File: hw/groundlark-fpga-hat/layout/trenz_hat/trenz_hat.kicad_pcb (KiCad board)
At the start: 2 copper layers, 120 parts

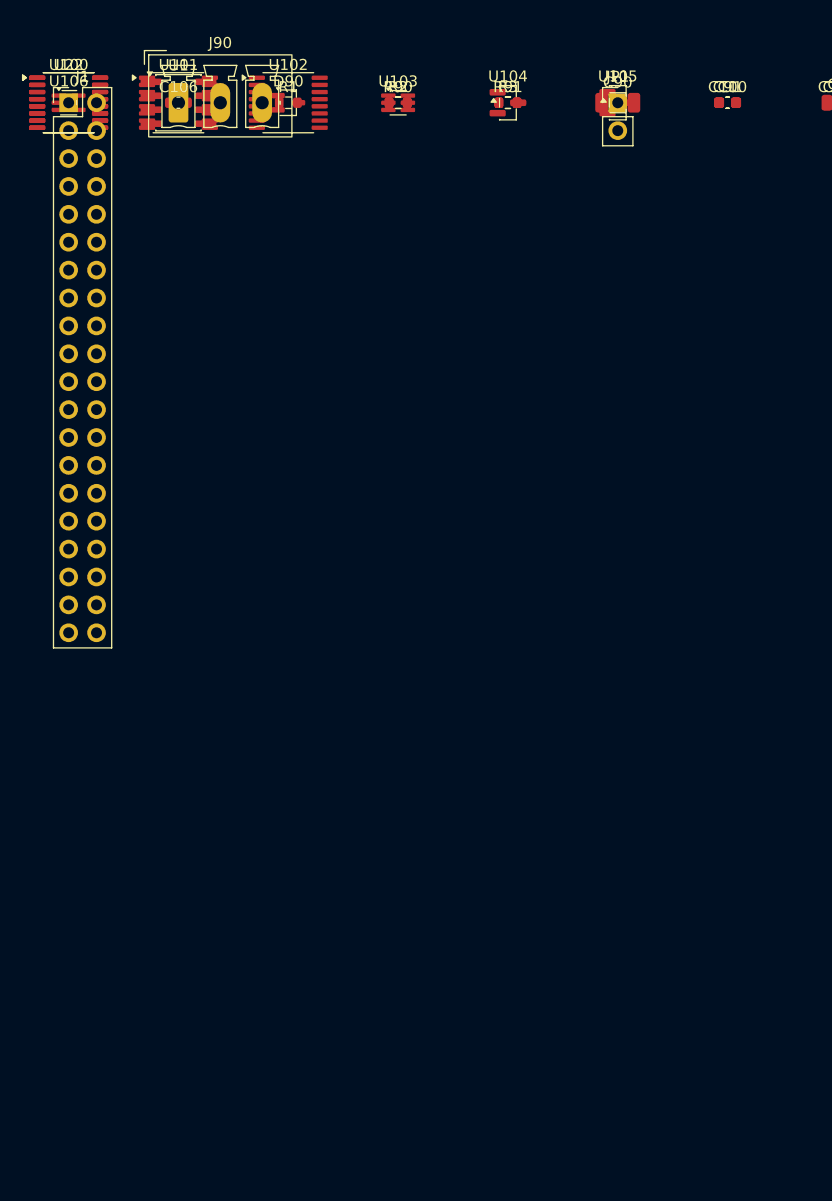
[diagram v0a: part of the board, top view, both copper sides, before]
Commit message: Use horizontal geophone connector and publish detailed enclosure render
Synchronize J90 routing, native SES, assembly mapping, enclosure fit, models and validation. Add a 4K clear-PETG README render and derive assembly PDF part identities from package procurement. Preserve Git-normalized source bindings and original validation/render input hashes. Generated JLCPCB packages remain local.
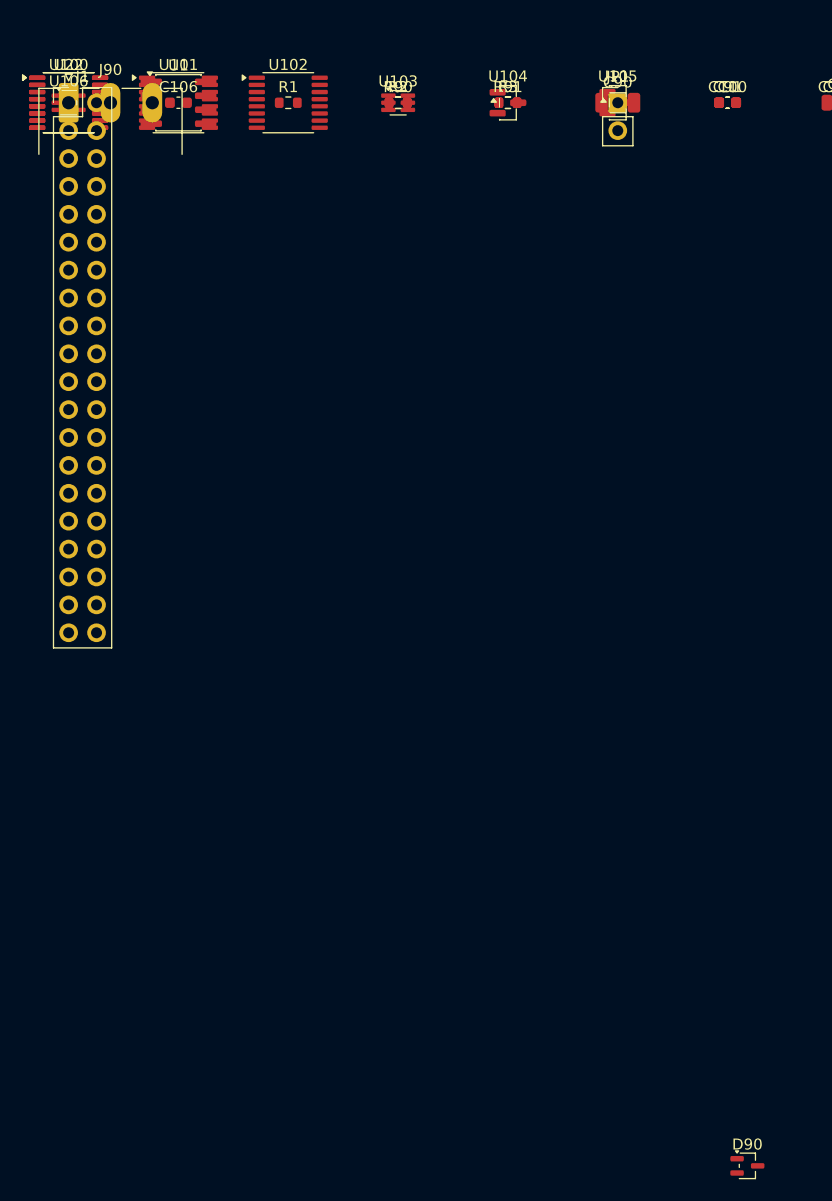
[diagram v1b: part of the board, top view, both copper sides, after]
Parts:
- J90: footprint elec:Connector_Phoenix_MC__PhoenixContact_MCV_1,5_3-G-3.81_1x03_P3.81mm_Vertical -> elec:Connector_Phoenix_MC__PhoenixContact_MC_1,5_3-G-3.81_1x03_P3.81mm_Horizontal
- moved D90 105.4 mm to (61.8, 96.8)
- moved J90 10.0 mm to (0.00, 0.00)

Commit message: Add TI Pi power supervision and expand DAQHAT enclosure
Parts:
- added C110: , elec:PWR_C_1210_3225Metric, F.Cu at (1350.0, 0.00)
- added C111: , elec:PWR_C_1210_3225Metric, F.Cu at (1360.0, 0.00)
- added C112: , elec:PWR_C_1210_3225Metric, F.Cu at (1370.0, 0.00)
- added C130: , elec:SUP_C_0805_2012Metric, F.Cu at (50.0, 0.00)
- added C131: , elec:PWR_C_1206_3216Metric, F.Cu at (60.0, 0.00)
- added C132: , elec:PWR_C_1206_3216Metric, F.Cu at (80.0, 0.00)
- added C133: , elec:PWR_C_1206_3216Metric, F.Cu at (90.0, 0.00)
- added C134: , elec:PWR_C_0603_1608Metric, F.Cu at (100.0, 0.00)
- added C135: , elec:PWR_CP_Elec_6.3x7.7, F.Cu at (110.0, 0.00)
- added C136: , elec:PWR_C_1210_3225Metric, F.Cu at (120.0, 0.00)
- added C137: , elec:PWR_C_1210_3225Metric, F.Cu at (130.0, 0.00)
- added C138: , elec:PWR_C_1210_3225Metric, F.Cu at (140.0, 0.00)
- added C139: , elec:SUP_C_0603_1608Metric, F.Cu at (190.0, 0.00)
- added C140: , elec:SUP_C_0805_2012Metric, F.Cu at (200.0, 0.00)
- added C141: , elec:PWR_C_0603_1608Metric, F.Cu at (230.0, 0.00)
- added C142: , elec:SUP_C_0805_2012Metric, F.Cu at (240.0, 0.00)
- added C143: , elec:SUP_C_0603_1608Metric, F.Cu at (250.0, 0.00)
- added C144: , elec:SUP_C_0603_1608Metric, F.Cu at (270.0, 0.00)
- added C145: , elec:SUP_C_0603_1608Metric, F.Cu at (300.0, 0.00)
- added C24: , elec:Capacitor_SMD__C_0603_1608Metric, F.Cu at (1190.0, 0.00)
- added C86: , elec:PWR_C_1206_3216Metric, F.Cu at (1310.0, 0.00)
- added C87: , elec:PWR_C_1206_3216Metric, F.Cu at (1320.0, 0.00)
- added C88: , elec:PWR_C_0603_1608Metric, F.Cu at (1330.0, 0.00)
- added C89: , elec:PWR_CP_Elec_6.3x7.7, F.Cu at (1340.0, 0.00)
- added D130: , elec:PWR_D_SMA, F.Cu at (20.0, 0.00)
- added D131: , elec:SUP_D_SMA, F.Cu at (30.0, 0.00)
- added D80: , elec:PWR_D_SMA, F.Cu at (1220.0, 0.00)
- added D81: , elec:PWR_D_SMA, F.Cu at (1230.0, 0.00)
- added F130: , elec:SUP_Fuse_1206_3216Metric, F.Cu at (10.0, 0.00)
- added J130: , elec:SUP_PhoenixContact_MC_1,5_2-G-3.81_1x02_P3.81mm_Horizontal, F.Cu at (0.00, 0.00)
- added J131: , elec:SUP_PinHeader_1x05_P1.27mm_Vertical, F.Cu at (370.0, 0.00)
- added JP130: , elec:SUP_PinHeader_1x02_P2.54mm_Vertical, F.Cu at (380.0, 0.00)
- added Q130: , elec:SUP_SOT-23, F.Cu at (310.0, 0.00)
- added Q131: , elec:SUP_SOT-23, F.Cu at (340.0, 0.00)
- added R120: , elec:PWR_R_0603_1608Metric, F.Cu at (1250.0, 0.00)
- added R121: , elec:PWR_R_0603_1608Metric, F.Cu at (1260.0, 0.00)
- added R122: , elec:PWR_R_0603_1608Metric, F.Cu at (1270.0, 0.00)
- added R123: , elec:PWR_R_0603_1608Metric, F.Cu at (1280.0, 0.00)
- added R124: , elec:PWR_R_0603_1608Metric, F.Cu at (1290.0, 0.00)
- added R130: , elec:PWR_R_0603_1608Metric, F.Cu at (150.0, 0.00)
- added R131: , elec:SUP_R_0603_1608Metric, F.Cu at (160.0, 0.00)
- added R132: , elec:PWR_R_0603_1608Metric, F.Cu at (170.0, 0.00)
- added R133: , elec:SUP_R_0603_1608Metric, F.Cu at (210.0, 0.00)
- added R134: , elec:SUP_R_0603_1608Metric, F.Cu at (260.0, 0.00)
- added R135: , elec:SUP_R_0603_1608Metric, F.Cu at (280.0, 0.00)
- added R136: , elec:SUP_R_0603_1608Metric, F.Cu at (290.0, 0.00)
- added R137: , elec:PWR_R_0603_1608Metric, F.Cu at (320.0, 0.00)
- added R138: , elec:PWR_R_0603_1608Metric, F.Cu at (330.0, 0.00)
- added R139: , elec:PWR_R_0603_1608Metric, F.Cu at (350.0, 0.00)
- added R140: , elec:PWR_R_0603_1608Metric, F.Cu at (360.0, 0.00)
- added R141: , elec:PWR_R_0603_1608Metric, F.Cu at (0.00, 0.00)
- added SW80: , elec:PWR_SW_SPDT_PCM12, F.Cu at (1300.0, 0.00)
- added U130: , elec:SUP_QFN-32-1EP_5x5mm_P0.5mm_EP3.45x3.45mm, F.Cu at (220.0, 0.00)
- added U131: , elec:SUP_SOT-23-5, F.Cu at (40.0, 0.00)
- added U132: , elec:PWR_Texas_B3QFN-14-1EP_5x5.5mm_P0.65mm, F.Cu at (70.0, 0.00)
- added U133: , elec:SUP_Texas_WSON10_DQC0010A, F.Cu at (180.0, 0.00)
- added U23: , elec:Groundlark__DLVR_E1BS, F.Cu at (1180.0, 0.00)
- added U80: , elec:PWR_Texas_B3QFN-14-1EP_5x5.5mm_P0.65mm, F.Cu at (1240.0, 0.00)
- F80: footprint elec:TZ_TZ_FUSE -> elec:PWR_Fuse_1206_3216Metric
- J83: footprint elec:TZ_TZ_POWER -> elec:PWR_BarrelJack_CUI_PJ-102AH_Horizontal
- moved C106 1160.0 mm to (1170.0, 0.00)
- moved U106 1160.0 mm to (1160.0, 0.00)
- moved C100 860.0 mm to (920.0, 0.00)
- moved C101 860.0 mm to (930.0, 0.00)
- moved C102 860.0 mm to (940.0, 0.00)
- moved C103 860.0 mm to (950.0, 0.00)
- moved C104 860.0 mm to (960.0, 0.00)
- moved C105 860.0 mm to (970.0, 0.00)
- moved R100 860.0 mm to (980.0, 0.00)
- moved R101 860.0 mm to (990.0, 0.00)
- moved R102 860.0 mm to (1000.0, 0.00)
- moved R103 860.0 mm to (1010.0, 0.00)
- moved R104 860.0 mm to (1020.0, 0.00)
- moved R105 860.0 mm to (1030.0, 0.00)
- moved R106 860.0 mm to (1040.0, 0.00)
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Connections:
- net EXT_3V3 renamed EXT_12V
- F80 pad 2: FPGA_VIN -> FUSED_12V
- J1 pad 31: 31 -> PI_SHUTDOWN_N
- J1 pad 33: 33 -> PI_HALTED
- J81 pad 31: j81-31 -> 31
- J81 pad 33: j81-33 -> 33

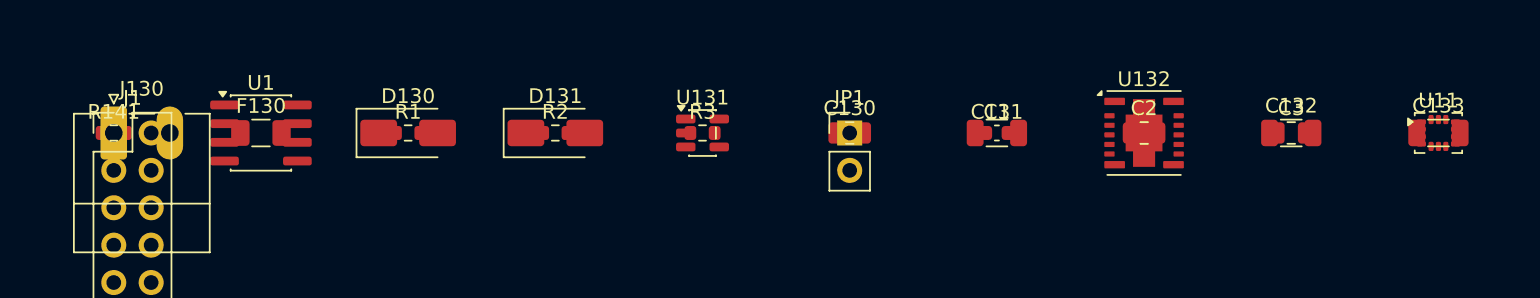
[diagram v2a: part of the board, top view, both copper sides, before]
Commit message: Add Groundlark GNSS timing, SMA access and calibration workflow
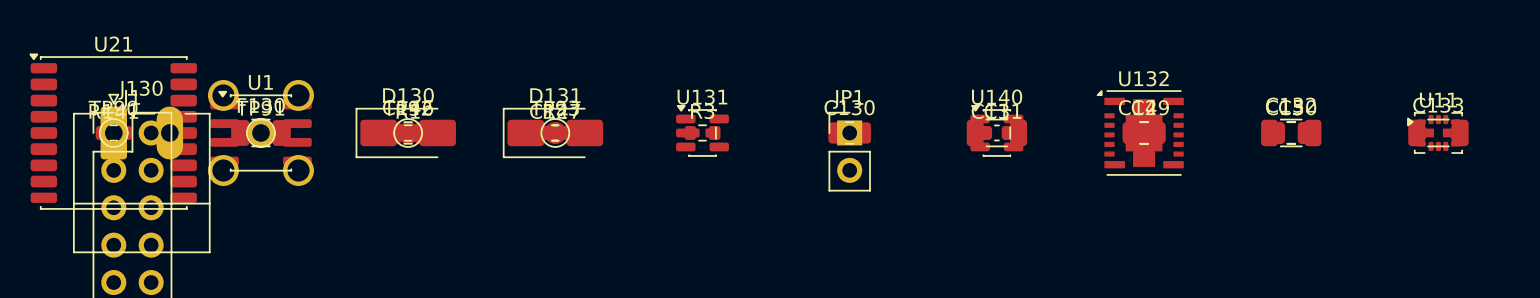
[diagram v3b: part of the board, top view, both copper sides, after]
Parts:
- added C146: , elec:Capacitor_SMD__C_0805_2012Metric, F.Cu at (20.0, 0.00)
- added C147: , elec:Capacitor_SMD__C_0603_1608Metric, F.Cu at (30.0, 0.00)
- added C148: , elec:GNSS_C0402, F.Cu at (40.0, 0.00)
- added C149: , elec:Capacitor_SMD__C_0805_2012Metric, F.Cu at (70.0, 0.00)
- added C150: , elec:Capacitor_SMD__C_0805_2012Metric, F.Cu at (80.0, 0.00)
- added D140: , elec:GNSS_SOD882, F.Cu at (90.0, 0.00)
- added J140: , elec:GNSS_HL_SMA_KWE_02, F.Cu at (10.0, 0.00)
- added L140: , elec:GNSS_L0402, F.Cu at (50.0, 0.00)
- added TP90: , elec:TestPoint__TestPoint_Pad_D1.5mm, F.Cu at (0.00, 0.00)
- added TP91: , elec:TestPoint__TestPoint_Pad_D1.5mm, F.Cu at (10.0, 0.00)
- added TP92: , elec:TestPoint__TestPoint_Pad_D1.5mm, F.Cu at (20.0, 0.00)
- added TP93: , elec:TestPoint__TestPoint_Pad_D1.5mm, F.Cu at (30.0, 0.00)
- added U140: , elec:SUP_SOT-23-5, F.Cu at (60.0, 0.00)
- added U21: , elec:RF_GPS__ublox_MAX, F.Cu at (0.00, 0.00)
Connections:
- J1 pad 18: 18 -> GNSS_PPS
- J80 pad 18: j80-18 -> 18

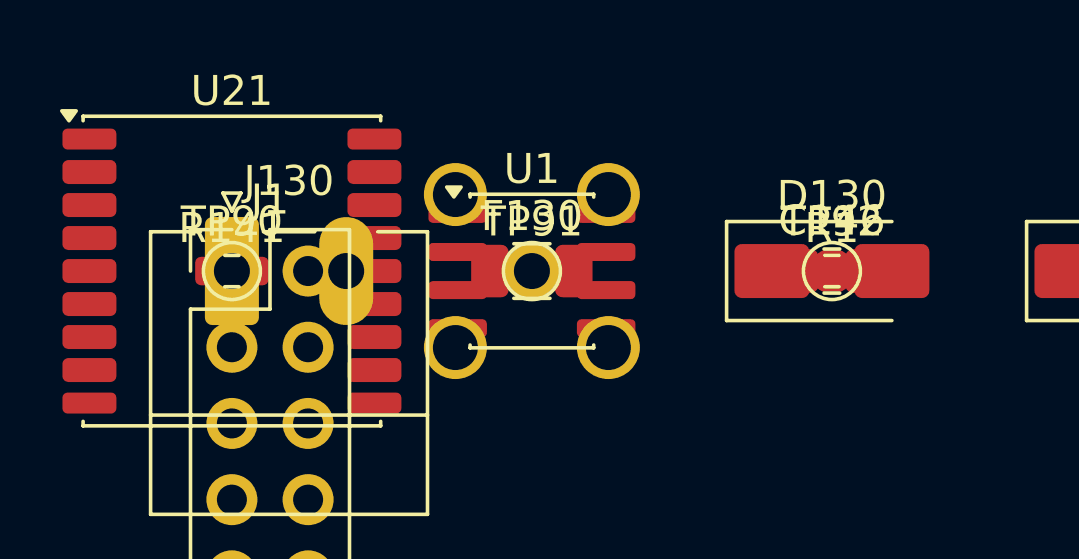
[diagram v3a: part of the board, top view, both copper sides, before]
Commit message: Fix Groundlark power and GNSS electrical faults
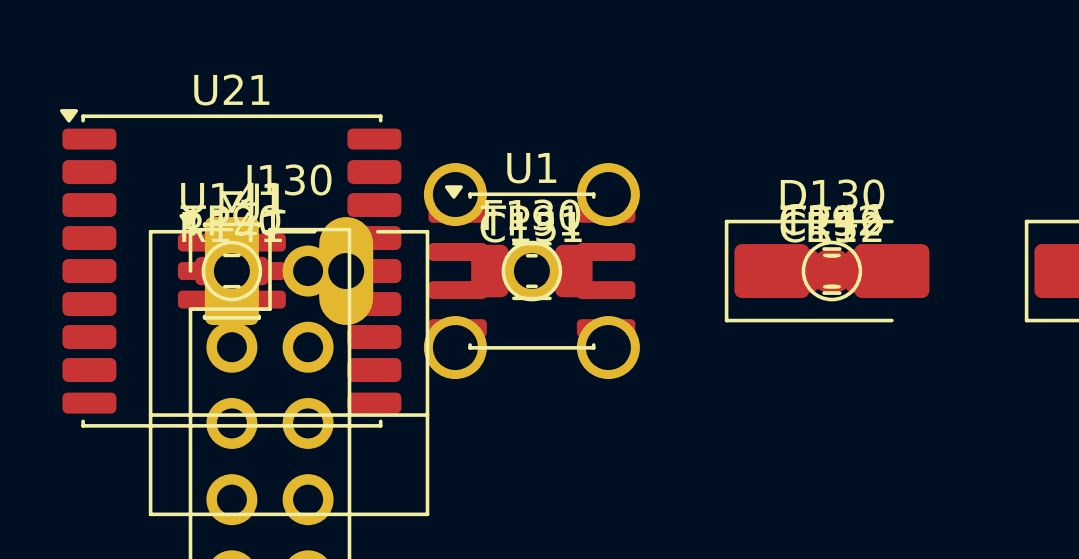
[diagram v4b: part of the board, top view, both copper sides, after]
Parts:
- added C151: , elec:SUP_C_0603_1608Metric, F.Cu at (10.0, 0.00)
- added C152: , elec:Capacitor_SMD__C_0603_1608Metric, F.Cu at (20.0, 0.00)
- added U141: , elec:GNSS_SOT23_6, F.Cu at (0.00, 0.00)
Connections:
- C150 pad 1: GNSS_BIAS -> GNSS_LDO
- C48 pad 1: PI_3V3 -> SENS_3V3
- C49 pad 1: SENS_3V3 -> PI_3V3
- U133 pad 7: u133-7 -> GND
- U140 pad 5: GNSS_BIAS -> GNSS_LDO
- U43 pad 1: PI_3V3 -> SENS_3V3
- U43 pad 2: PI_I2C_SDA -> I2C_SDA
- U43 pad 3: PI_I2C_SCL -> I2C_SCL
- U43 pad 6: I2C_SCL -> PI_I2C_SCL
- U43 pad 7: I2C_SDA -> PI_I2C_SDA
- U43 pad 8: SENS_3V3 -> PI_3V3
